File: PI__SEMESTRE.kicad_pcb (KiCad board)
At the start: 2 copper layers, 32 parts, among them IC1 LMV358IDR, J1 CX90B-16P1, U1 AMS1117, U11 ESP32-S3-WROOM-1, U14 BME688, U9 GUVA-S12SD

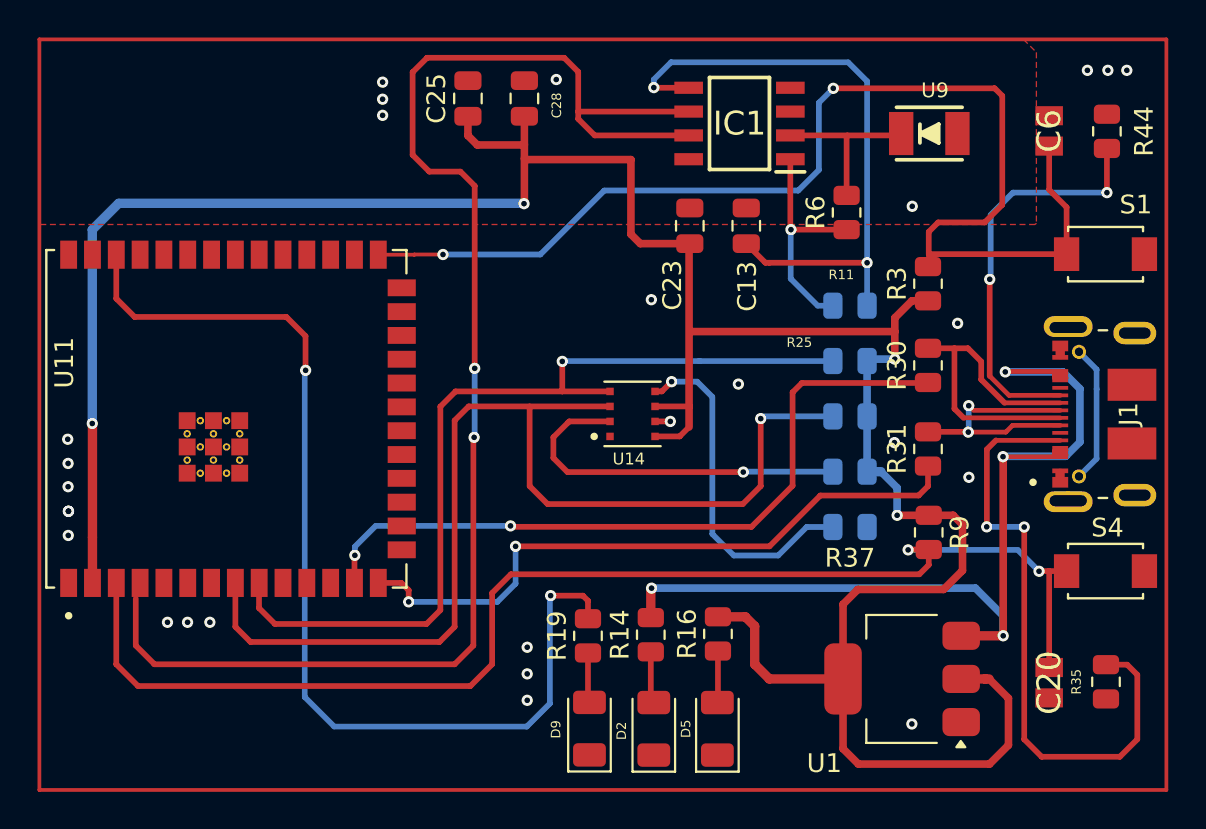
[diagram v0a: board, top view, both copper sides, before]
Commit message: se corrigieron muchoss errores tanto que al diseño pcb le hacian falta 4 capacitores porque no tenian huella suministrada, se hicieron cambios de serigrafia, se acomodaron algunos errores tanto de las pistas del usb-c, tambien se agregaron zonas de proteccion contra ruido para los componentes analogos.
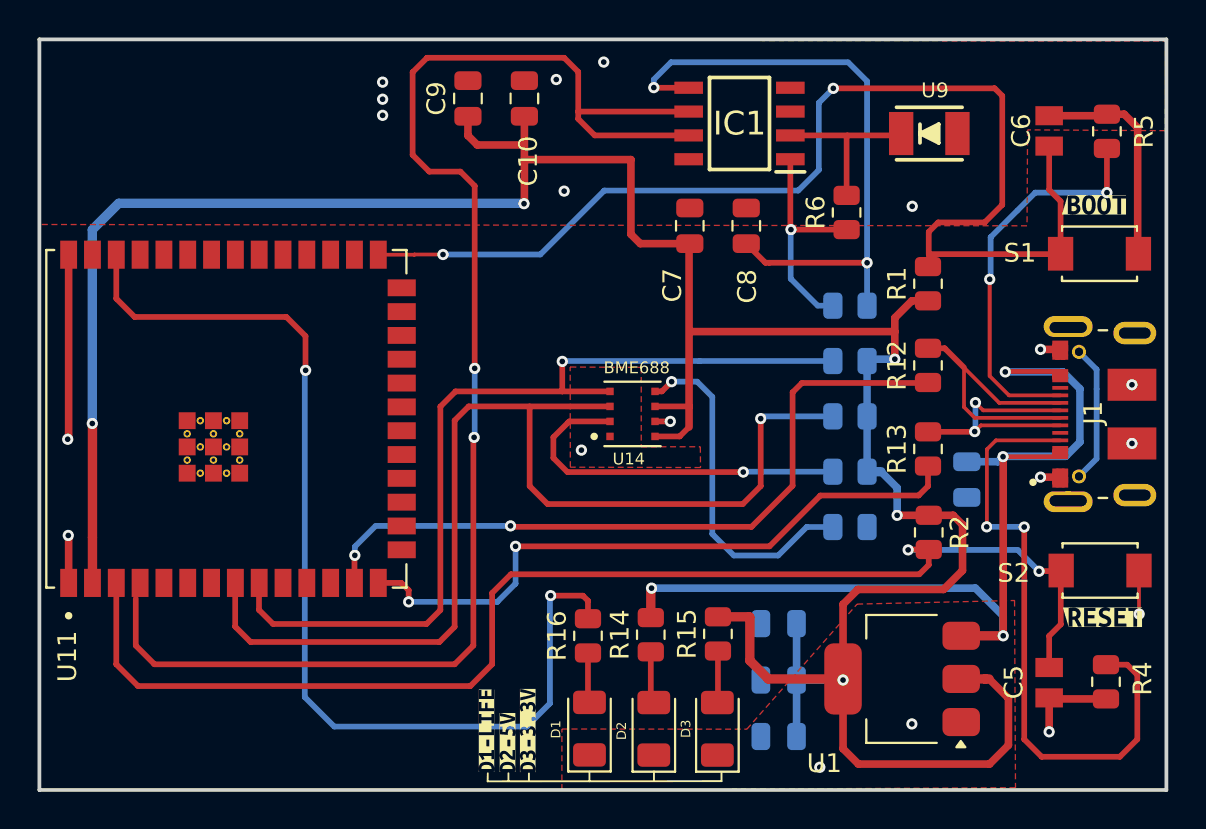
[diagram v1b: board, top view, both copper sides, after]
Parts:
- added C1: 100u, Capacitor_SMD:C_0805_2012Metric, B.Cu at (118.3, 81.7)
- added C2: 10u, Capacitor_SMD:C_0805_2012Metric, B.Cu at (108.3, 89.3)
- added C3: 22u, Capacitor_SMD:C_0805_2012Metric, B.Cu at (108.3, 92.3)
- added C4: 100n, Capacitor_SMD:C_0805_2012Metric, B.Cu at (108.3, 95.3)
- added kibuzzard-6A0FC95D: G***, kibuzzard-6A0FC95D, F.Cu at (94.9, 95.0)
- added kibuzzard-6A0FC9A7: G***, kibuzzard-6A0FC9A7, F.Cu at (93.8, 95.7)
- added kibuzzard-6A0FC9CC: G***, kibuzzard-6A0FC9CC, F.Cu at (92.7, 95.0)
- added kibuzzard-6A0FCD51: G***, kibuzzard-6A0FCD51, F.Cu at (125.1, 67.0)
- added kibuzzard-6A0FCD67: G***, kibuzzard-6A0FCD67, F.Cu at (125.5, 89.0)
- D1: renamed from D9; value LED VIVO -> LED
- D2: value LED 5V -> LED
- D3: renamed from D5; value LED 3.3V -> LED
- U11: footprint SamacSys_Parts:XCVR_ESP32-S3-WROOM-1U-N16R8 -> ESP32-S3-N16R8:XCVR_ESP32-S3-WROOM-1U-N16R8
- U9: footprint SamacSys_Parts:GUVA-S12SD -> GUVA-S12SD:GUVA-S12SD
- moved S1 0.32 mm to (125.4, 69.6)
- moved S2 0.29 mm to (125.4, 86.5)
- renumbered C28 to C10, C20 to C5, C23 to C7, C13 to C8, C25 to C9, R3 to R1, R40 to R10, R37 to R11, R30 to R12, R31 to R13, R16 to R15, R19 to R16, R9 to R2, R35 to R4, R44 to R5, R11 to R7, R24 to R8, R25 to R9, S4 to S2
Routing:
- net GND: track 1.74 -> 33.8 mm, vias 27 -> 19
- net +3.3V: track 152.5 -> 161.2 mm, vias 4 -> 5
- net D-: track 18.0 -> 15.7 mm
- net +5V: track 51.7 -> 53.7 mm
- net Boot: track 64.9 -> 63.8 mm
- net Net-(J1-CC2): track 21.9 -> 21.2 mm
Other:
- board outline added: 60.1 x 40 mm

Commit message: fix: se solucionan algunos errores de clearance y planos de tierra
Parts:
- R7: moved to F.Cu
- turned R7 to 0 degrees
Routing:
- net GND: track 33.8 -> 2.11 mm, vias 19 -> 22
- net Filtro: track 33.3 -> 28.7 mm, vias 2 -> 3
- net Boot: track 63.8 -> 60.3 mm
- net +5V: track 53.7 -> 56.9 mm
- net D-: track 15.7 -> 17.5 mm
- net +3.3V: track 161.2 -> 162.6 mm

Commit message: se voltean las resistencias de la cara de abajo
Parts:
- C1, R10, R11, R8, R9: moved to F.Cu
- moved R2 4.64 mm to (112.1, 86.4), turned to 180 degrees
- moved C1 3.01 mm to (117.3, 84.5)
- turned R7 to 180 degrees
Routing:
- net Filtro: track 28.7 -> 33.6 mm
- net +3.3V: track 162.6 -> 158.3 mm
- net +5V: track 56.9 -> 59.8 mm, vias 4 -> 5
- net EN: track 69.0 -> 67.4 mm
- net Net-(U14-SDO): track 18.4 -> 19.0 mm, vias 1 -> 2
- net I2C_SDA: track 59.2 -> 59.8 mm, vias 1 -> 2
- net Net-(U14-CSB): vias 1 -> 2
- net I2C_SCL: vias 1 -> 2

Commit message: se corrigio lo que sugerio el docente, pasando los componentes que estaban en la parte de atras de la placa
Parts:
- C2, C3, C4: moved to F.Cu
- moved C4 30.7 mm to (77.5, 95.0), turned to 0 degrees
- moved C3 14.0 mm to (94.5, 90.0), turned to 90 degrees
- moved C2 0.25 mm to (108.5, 89.5), turned to 90 degrees
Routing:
- net +3.3V: track 158.3 -> 209.6 mm, vias 5 -> 7

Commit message: se agrega nuestro logo se hacen las ultimos cambios para mandar hacer la pcb
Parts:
- added G***: LOGO, Logo-Ghost:E-Logo-Grupo_De_Los-Incapaces-10x10mm_, F.Cu at (75.9, 63.0)
- moved C1 0.45 mm to (117.7, 84.5)
- moved R2 0.24 mm to (112.1, 86.7)
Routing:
- net +5V: track 59.8 -> 62.8 mm
- net +3.3V: track 209.6 -> 208.8 mm
- net GND: vias 22 -> 44
